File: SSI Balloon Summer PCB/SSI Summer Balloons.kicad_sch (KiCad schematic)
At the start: 0 parts

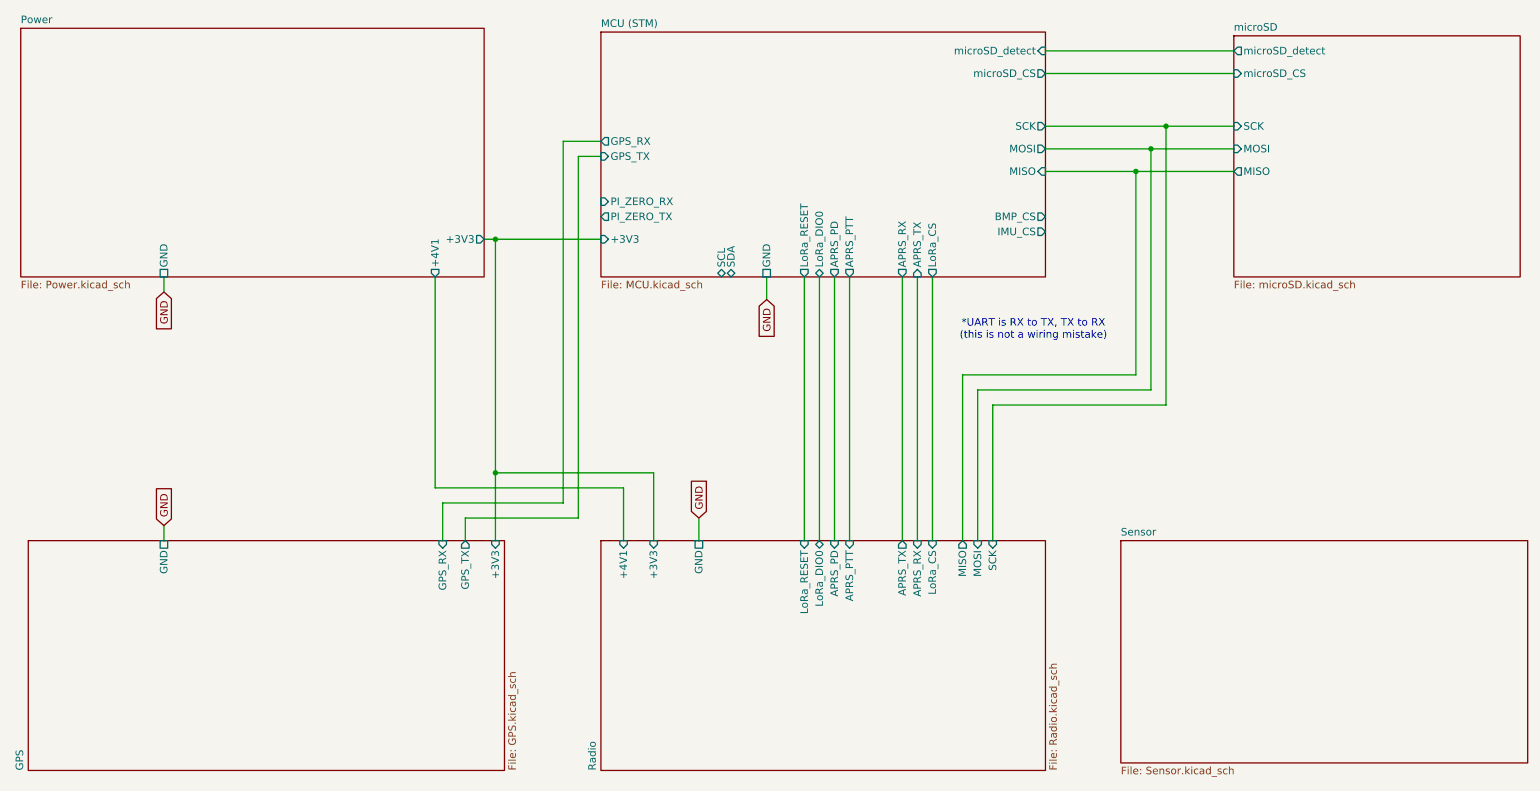
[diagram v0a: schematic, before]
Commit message: Finished sensors + tidied up schematic
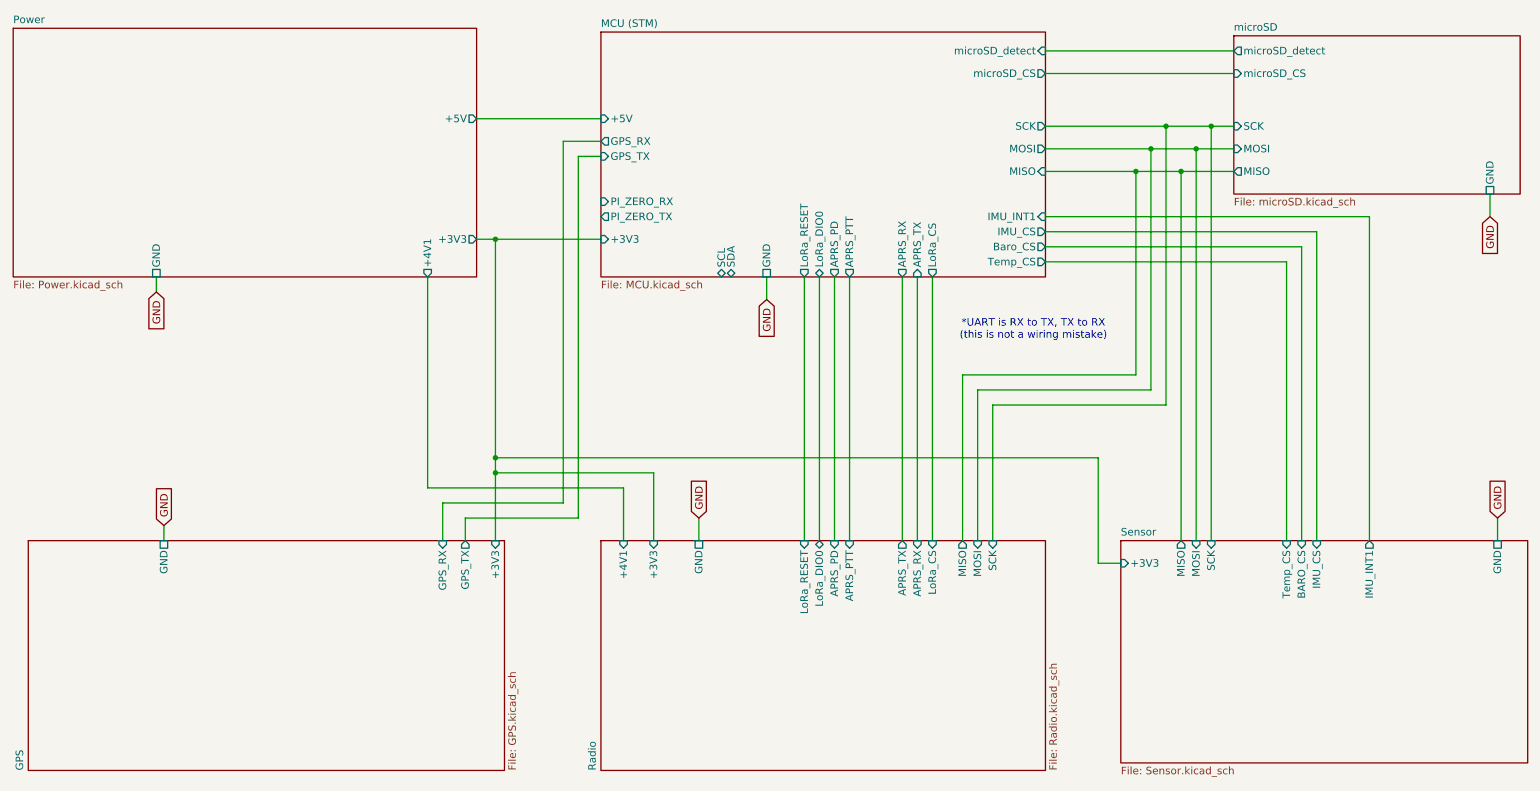
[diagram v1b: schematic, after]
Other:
- sheet MCU (STM) ports: added +5V, Baro_CS, IMU_INT1, Temp_CS; removed BMP_CS
- sheet Power ports: added +5V; removed none
- sheet Sensor ports: added +3V3, BARO_CS, GND, IMU_CS, IMU_INT1, MISO, MOSI, SCK, Temp_CS; removed none
- sheet microSD ports: added GND; removed none

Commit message: tidying
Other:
- sheet MCU (STM) ports: added none; removed PI_ZERO_RX, PI_ZERO_TX, SCL, SDA
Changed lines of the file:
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@@
-			)
-		)
-		(pin "PI_ZERO_RX" input
-			(at 116.84 63.5 180)
-			(effects
-				(font
-					(size 1.27 1.27)
-				)
-				(justify left)
 			)
 		)
@@
 				)
 				(justify right)
-			)
-		)
-		(pin "PI_ZERO_TX" output
-			(at 116.84 66.04 180)
-			(effects
-				(font
-					(size 1.27 1.27)
-				)
-				(justify left)
 			)
 		)
@@
 			(effects
 				(font
-					(size 1.27 1.27)
-				)
-				(justify left)
-			)
-		)
-		(pin "SCL" bidirectional
-			(at 137.16 76.2 270)
-			(effects
-				(font
-					(size 1.27 1.27)
-				)
-				(justify left)
-			)
-		)
-		(pin "SDA" bidirectional
-			(at 138.7793 76.2 270)
-			(effects
-				(font

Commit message: Added APRS_AUDIO
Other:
- sheet MCU (STM) ports: added APRS_AUDIO; removed none
- sheet Radio ports: added APRS_AUDIO; removed none
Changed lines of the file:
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@@
+	(wire
+		(pts
+			(xy 140.97 76.2) (xy 140.97 120.65)
+		)
+		(stroke
+			(width 0)
+			(type default)
+		)
+	)
 	(wire
 		(pts
@@
 			)
 		)
+		(pin "APRS_AUDIO" input
+			(at 140.97 120.65 90)
+			(effects
+				(font
+					(size 1.27 1.27)
+				)
+				(justify right)
+			)
+		)
 		(instances
 			(project "SSI Summer Balloons"
@@
 			(effects
 				(font
+					(size 1.27 1.27)
+				)
+				(justify left)
+			)
+		)
+		(pin "APRS_AUDIO" output
+			(at 140.97 76.2 270)
+			(effects
+				(font

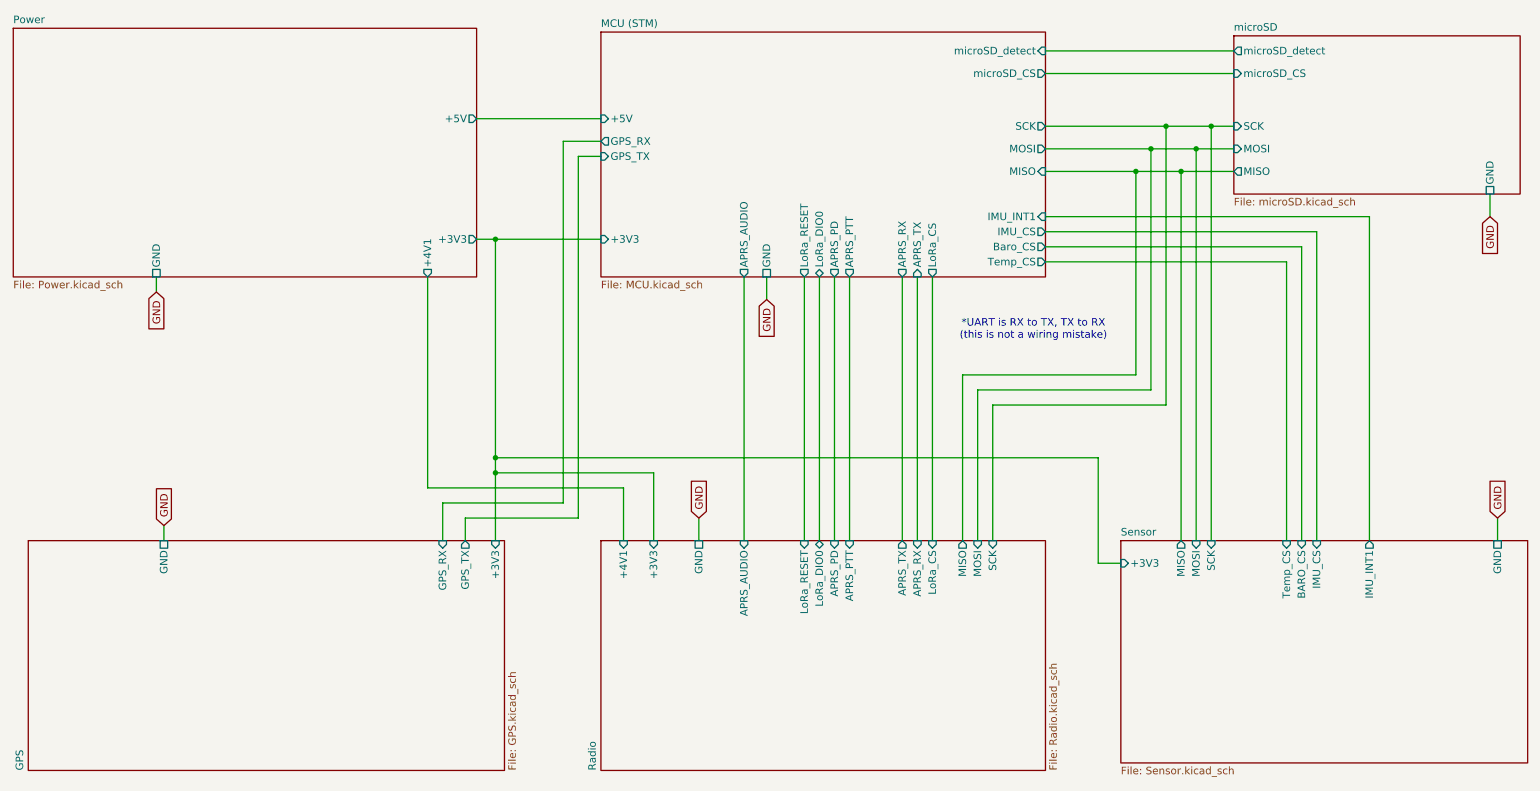
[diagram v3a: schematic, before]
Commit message: Minor tweaks, renamed some pins
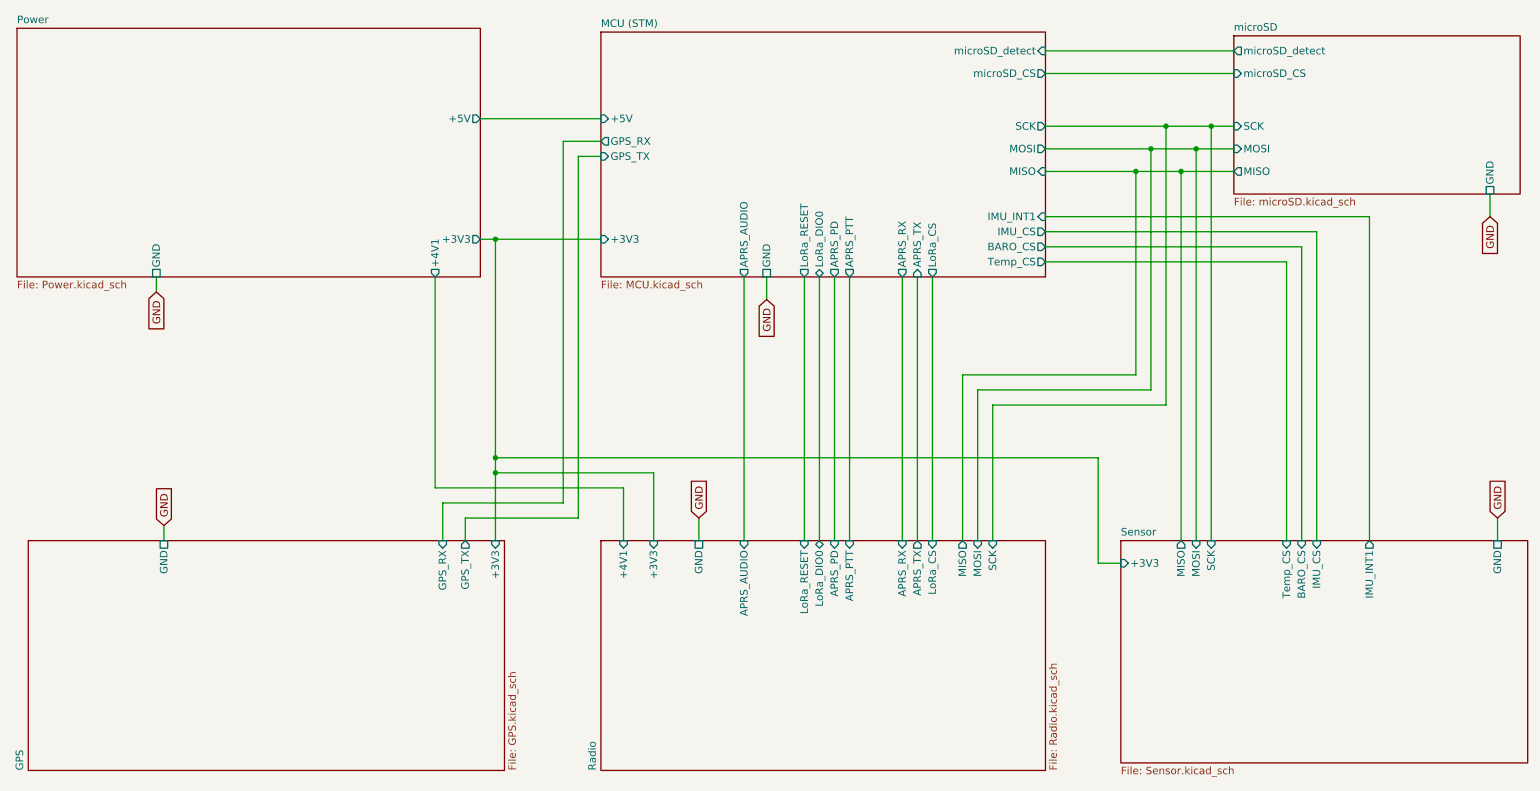
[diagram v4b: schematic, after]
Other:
- sheet MCU (STM) ports: added BARO_CS; removed Baro_CS
- note removed: "*UART is RX to TX, TX to RX (this is not a wiring mistake)"

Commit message: Overhauled power symbols for consistency and ERC
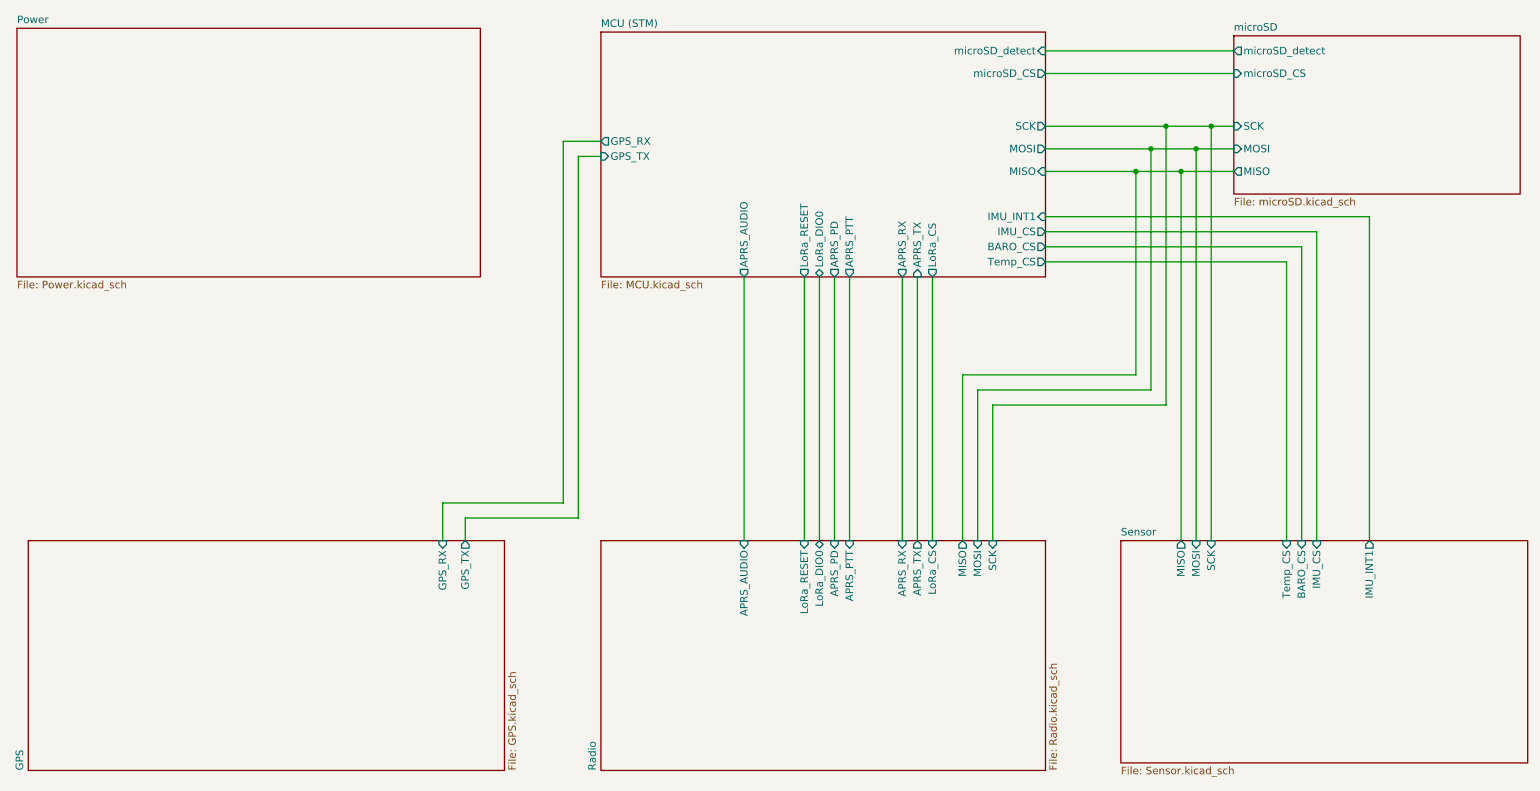
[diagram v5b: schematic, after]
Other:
- sheet GPS ports: added none; removed +3V3, GND
- sheet MCU (STM) ports: added none; removed +3V3, +5V, GND
- sheet Power ports: added none; removed +3V3, +4V1, +5V, GND
- sheet Radio ports: added none; removed +3V3, +4V1, GND
- sheet Sensor ports: added none; removed +3V3, GND
- sheet microSD ports: added none; removed GND
